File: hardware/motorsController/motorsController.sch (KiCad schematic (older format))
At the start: 11 parts, among them J1 batery_connector, J10 batery_connector, J2 Screw_Terminal_01x01, J3 Screw_Terminal_01x01, J4 Screw_Terminal_01x01, J5 Screw_Terminal_01x01, J6 Screw_Terminal_01x01, J7 Screw_Terminal_01x01, J8 Screw_Terminal_01x01, J9 Screw_Terminal_01x01

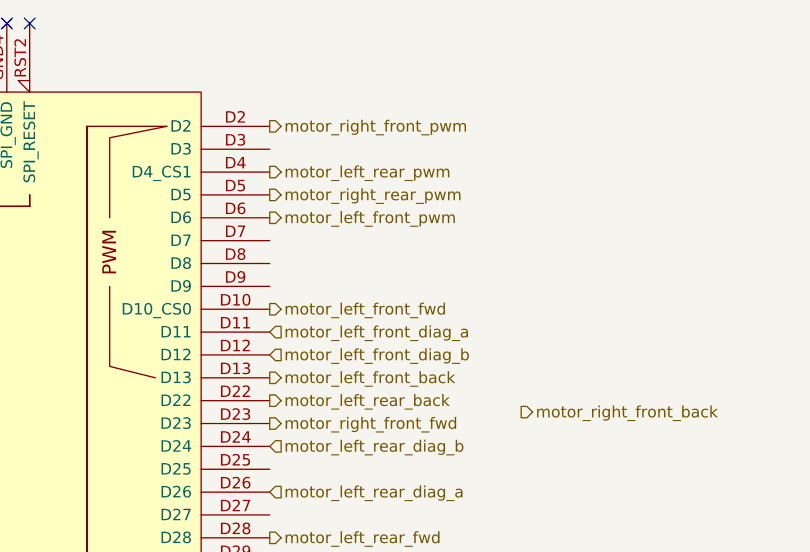
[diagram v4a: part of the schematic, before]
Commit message: move left-front driver four pins right
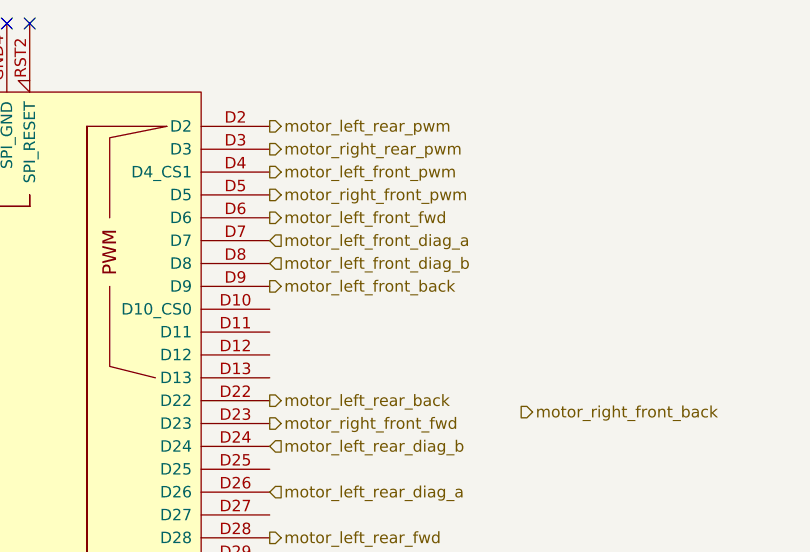
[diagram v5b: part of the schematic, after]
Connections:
- net motor_left_front_back: now also XA1.D9; no longer XA1.D13
- net motor_left_front_diag_a: now also XA1.D7; no longer XA1.D11
- net motor_left_front_diag_b: now also XA1.D8; no longer XA1.D12
- net motor_left_front_fwd: now also XA1.D6; no longer XA1.D10 (D10_CS0)
- net motor_left_front_pwm: now also XA1.D4 (D4_CS1); no longer XA1.D6
- net motor_left_rear_pwm: now also XA1.D2; no longer XA1.D4 (D4_CS1)
- net motor_right_front_pwm: now also XA1.D5; no longer XA1.D2
- net motor_right_rear_pwm: now also XA1.D3; no longer XA1.D5
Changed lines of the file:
@@
 Text HLabel 4000 2400 2    50   Output ~ 0
 motor_right_front_diag_a
-Text HLabel 14600 1350 2    50   Output ~ 0
+Text HLabel 14600 1650 2    50   Output ~ 0
 motor_right_front_pwm
 Text HLabel 15700 2600 2    50   Output ~ 0
@@
 Text HLabel 12000 3350 0    50   Input ~ 0
 motor_left_rear_cs
-Text HLabel 14600 2450 2    50   Output ~ 0
-motor_left_front_back
-Text HLabel 14600 2150 2    50   Output ~ 0
-motor_left_front_fwd
 Text HLabel 14600 3950 2    50   Output ~ 0
 motor_right_rear_fwd
@@
 Text HLabel 14600 3150 2    50   Output ~ 0
 motor_left_rear_fwd
-Text HLabel 14600 2350 2    50   Input ~ 0
-motor_left_front_diag_b
-Text HLabel 14600 2250 2    50   Input ~ 0
-motor_left_front_diag_a
 Text HLabel 14600 3550 2    50   Input ~ 0
 motor_right_rear_diag_b
 Text HLabel 14600 3750 2    50   Input ~ 0
 motor_right_rear_diag_a
-Text HLabel 14600 1750 2    50   Output ~ 0
+Text HLabel 14600 1550 2    50   Output ~ 0
 motor_left_front_pwm
-Text HLabel 14600 1650 2    50   Output ~ 0
+Text HLabel 14600 1450 2    50   Output ~ 0
 motor_right_rear_pwm
-Text HLabel 14600 1550 2    50   Output ~ 0
+Text HLabel 14600 1350 2    50   Output ~ 0
 motor_left_rear_pwm
 $Comp
@@
 Text HLabel 14600 3350 2    50   Output ~ 0
 motor_right_rear_back
+Text HLabel 14600 1850 2    50   Input ~ 0
+motor_left_front_diag_a
+Text HLabel 14600 1950 2    50   Input ~ 0
+motor_left_front_diag_b
+Text HLabel 14600 1750 2    50   Output ~ 0
+motor_left_front_fwd
+Text HLabel 14600 2050 2    50   Output ~ 0
+motor_left_front_back
 $EndSCHEMATC

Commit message: connect right-front driver to arduino
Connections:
- net motor_right_front_back: now also XA1.D13
- net motor_right_front_diag_a: now also XA1.D11
- net motor_right_front_diag_b: now also XA1.D12; no longer XA1.D31
- net motor_right_front_fwd: now also XA1.D10 (D10_CS0); no longer XA1.D23
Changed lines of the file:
@@
 Text HLabel 14600 1650 2    50   Output ~ 0
 motor_right_front_pwm
-Text HLabel 15700 2600 2    50   Output ~ 0
+Text HLabel 14600 2450 2    50   Output ~ 0
 motor_right_front_back
-Text HLabel 14600 2650 2    50   Output ~ 0
+Text HLabel 14600 2150 2    50   Output ~ 0
 motor_right_front_fwd
 Text HLabel 12000 3050 0    50   Input ~ 0
 motor_right_front_cs
-Text HLabel 14600 3450 2    50   Input ~ 0
+Text HLabel 14600 2350 2    50   Input ~ 0
 motor_right_front_diag_b
-Text HLabel 15700 3250 2    50   Input ~ 0
+Text HLabel 14600 2250 2    50   Input ~ 0
 motor_right_front_diag_a
 $Comp

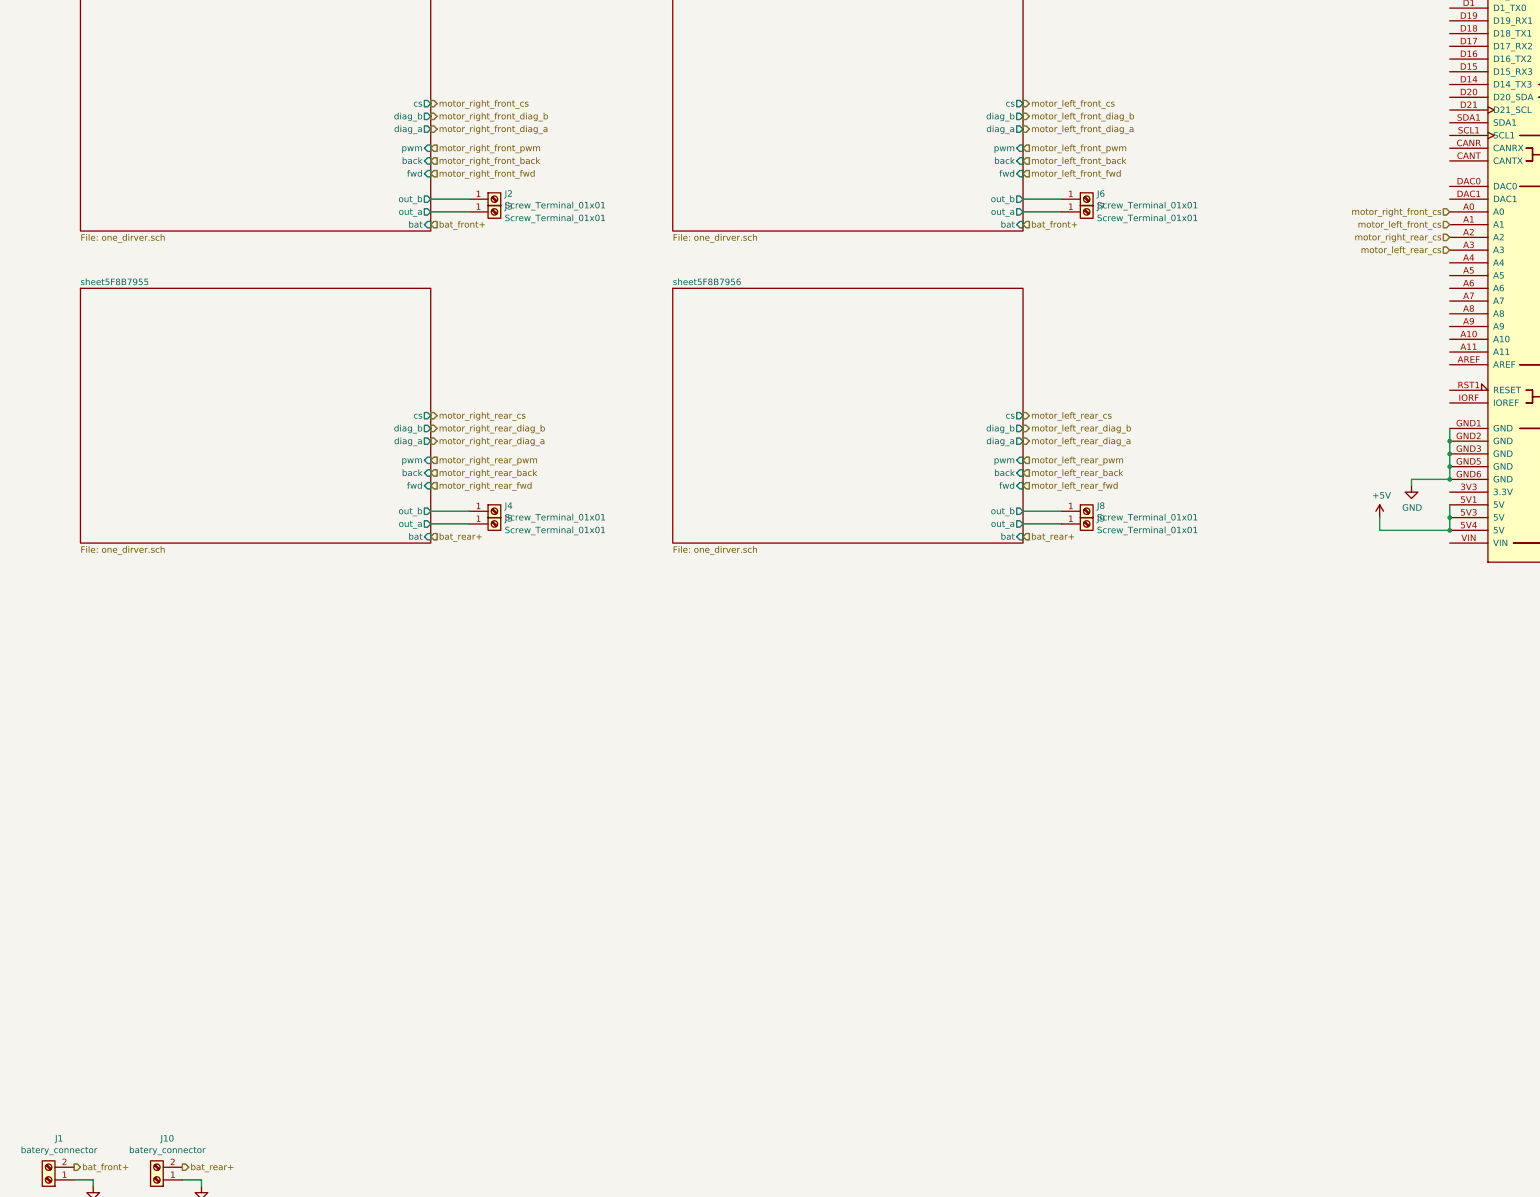
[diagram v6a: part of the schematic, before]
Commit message: add an i2c connector
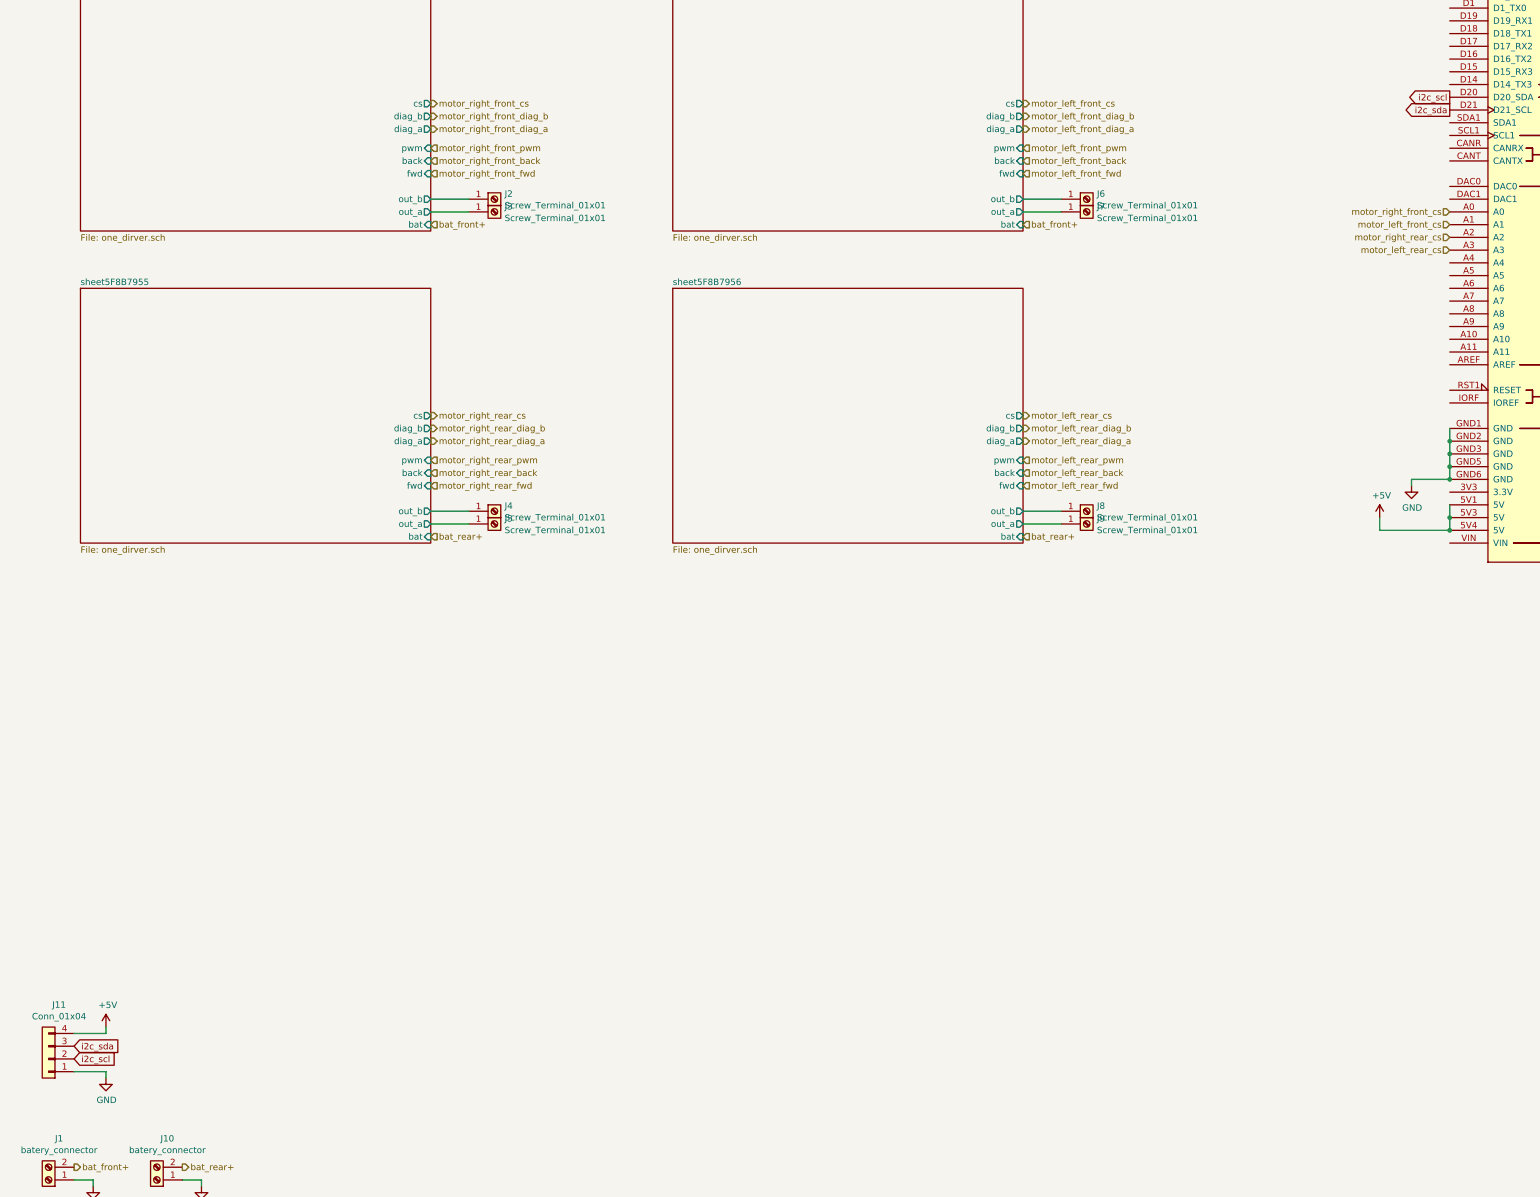
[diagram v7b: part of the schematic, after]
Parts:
- added J11: Conn_01x04, Connector_PinHeader_1.00mm:PinHeader_1x04_P1.00mm_Vertical, symbol Connector_Generic:Conn_01x04
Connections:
- net +5V: now also J11.4 (Pin_4)
- net GND: now also J11.1 (Pin_1)
- net i2c_scl: now reaches XA1.D20 (D20_SDA)
- net i2c_scl: now also J11.2 (Pin_2)
- net i2c_sda: now reaches XA1.D21 (D21_SCL)
- net i2c_sda: now also J11.3 (Pin_3)
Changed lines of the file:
@@
 Text HLabel 14600 2050 2    50   Output ~ 0
 motor_left_front_back
+Text GLabel 1200 9700 2    50   Input ~ 0
+i2c_scl
+Text GLabel 1200 9600 2    50   Input ~ 0
+i2c_sda
+$Comp
+L power:+5V #PWR0121
+U 1 1 5FAD9AB3
+P 1450 9450
+F 0 "#PWR0121" H 1450 9300 50  0001 C CNN
+F 1 "+5V" H 1465 9623 50  0000 C CNN
+F 2 "" H 1450 9450 50  0001 C CNN
+F 3 "" H 1450 9450 50  0001 C CNN
+	1    1450 9450
+	1    0    0    -1
+$EndComp
+Wire Wire Line
+	1450 9450 1450 9500
+Wire Wire Line
+	1450 9500 1200 9500
+$Comp
+L power:GND #PWR0122
+U 1 1 5FADB6FB
+P 1450 9850
+F 0 "#PWR0122" H 1450 9600 50  0001 C CNN
+F 1 "GND" H 1455 9677 50  0000 C CNN
+F 2 "" H 1450 9850 50  0001 C CNN
+F 3 "" H 1450 9850 50  0001 C CNN
+	1    1450 9850
+	1    0    0    -1
+$EndComp
+Wire Wire Line
+	1450 9850 1450 9800
+Wire Wire Line
+	1450 9800 1200 9800
+Text GLabel 12000 2150 0    50   Output ~ 0
+i2c_scl
+Text GLabel 12000 2250 0    50   Output ~ 0
+i2c_sda
+$Comp
+L Connector_Generic:Conn_01x04 J11
+U 1 1 5FAD5301
+P 1000 9700
+F 0 "J11" H 918 9275 50  0000 C CNN
+F 1 "Conn_01x04" H 918 9366 50  0000 C CNN
+F 2 "Connector_PinHeader_1.00mm:PinHeader_1x04_P1.00mm_Vertical" H 1000 9700 50  0001 C CNN
+F 3 "~" H 1000 9700 50  0001 C CNN
+	1    1000 9700
+	-1   0    0    1
+$EndComp
 $EndSCHEMATC
